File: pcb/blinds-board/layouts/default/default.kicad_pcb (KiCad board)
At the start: 6 copper layers, 38 x 81 mm, 87 parts

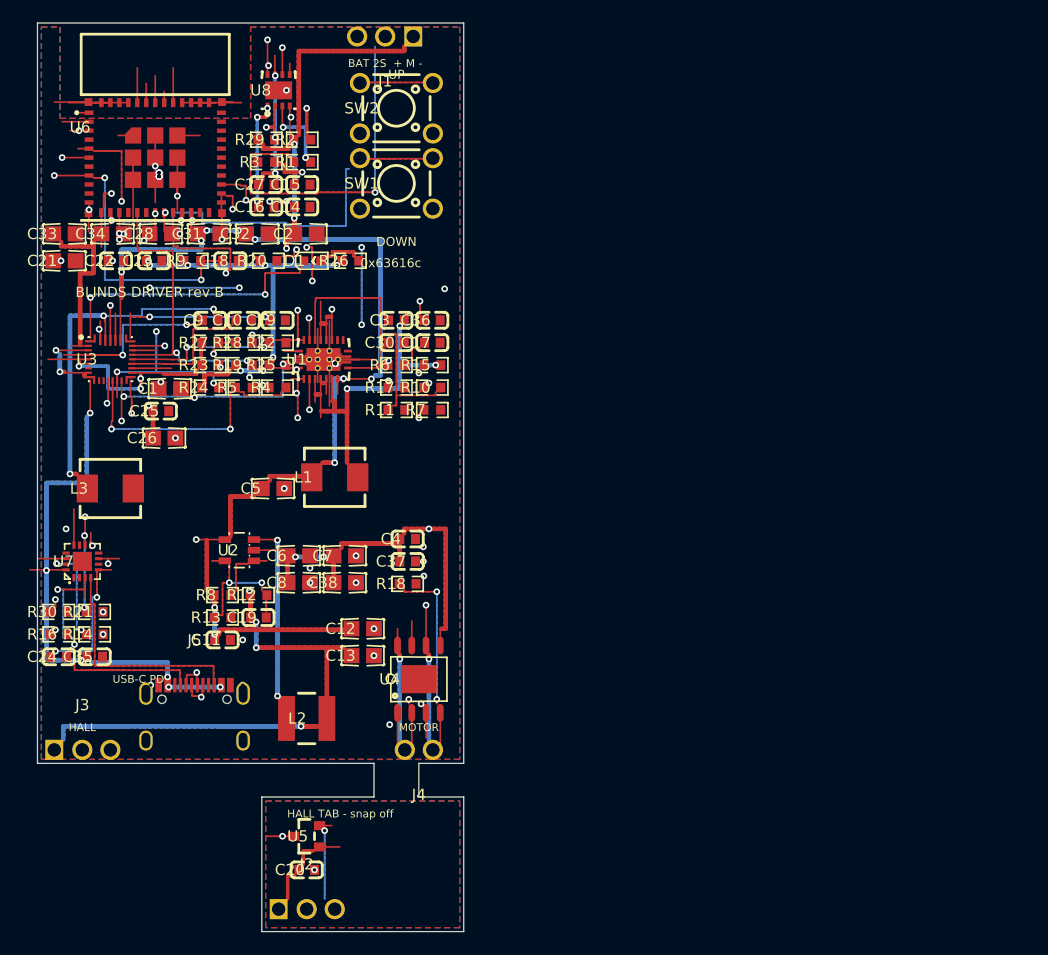
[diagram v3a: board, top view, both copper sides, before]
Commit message: feat(blinds-pcb): rev C — 88x32 flat board for the v2 center-drop unit
Board reshaped to lie flat on the enclosure floor: buttons + USB-C out
the front edge (unit x 38/49/60), hall tab moves below the board
(panel 88x47), 3x M3 mount holes + a B.Cu keep-out where the enclosure
pillar presses under the USB. Charger rotated 180 so its SW pins face
the inductor; flank passives mirrored to match; per-pad fanout
staggers re-derived (rev B's were orientation-specific). Netless pad
halos widened to via-hole clearance. Fully routed: 62 nets, ~10.2k
segments, 249 vias, zero unrouted.

KiCad DRC: 35 violations — SAME classes and slightly fewer than the
committed rev B board scores under today's harness (39), including the
identical 4 padstack_invalid on the BQ25798 corner pads and the
unconnected-pads artifact class. The DRC gate in build_outputs.sh
cannot currently pass on either rev; needs its own investigation
before gerbers.
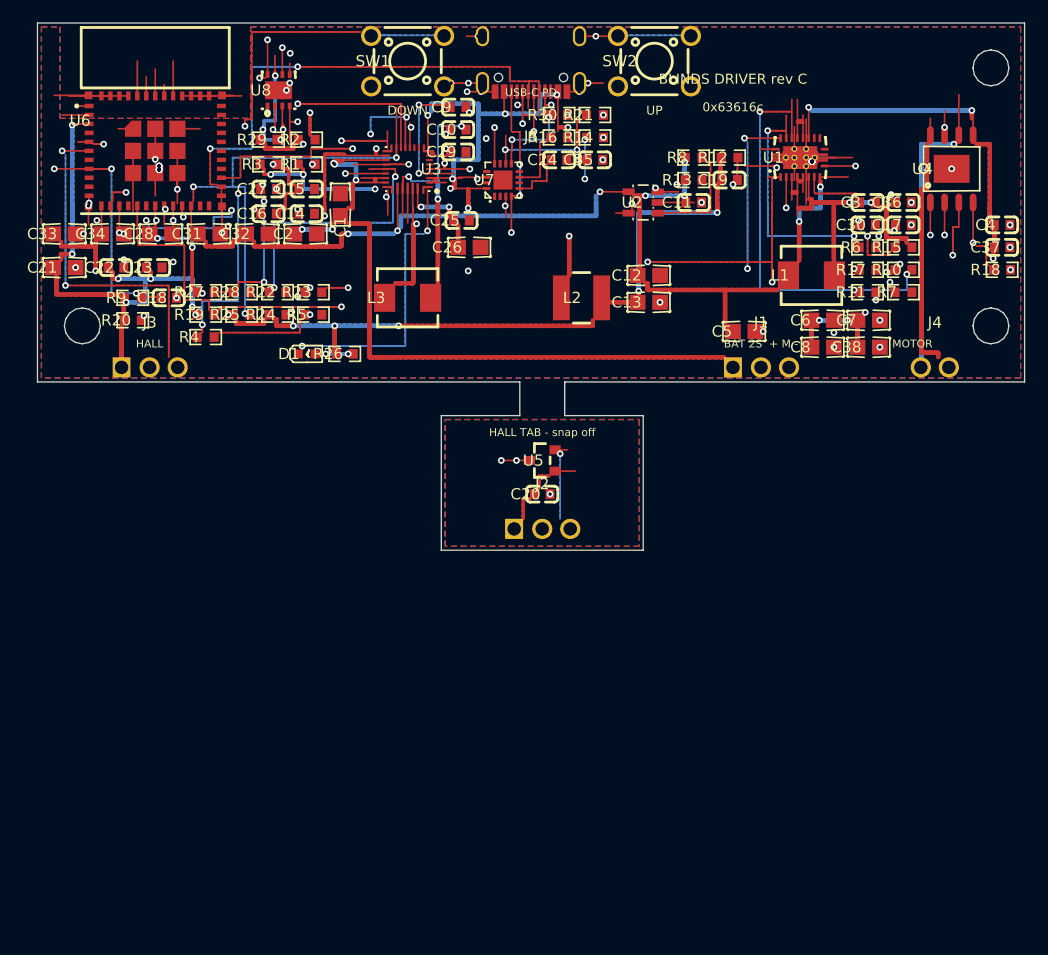
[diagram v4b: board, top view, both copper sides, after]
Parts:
- moved U4 65.8 mm to (81.5, 13.0)
- moved J5 65.2 mm to (44.0, 3.65), turned to 180 degrees
- moved C24 62.9 mm to (46.5, 12.2)
- moved C35 62.9 mm to (49.7, 12.2)
- moved R14 62.9 mm to (49.7, 10.2)
- moved R16 62.9 mm to (46.5, 10.2)
- moved R21 62.9 mm to (49.7, 8.20)
- moved R30 62.9 mm to (46.5, 8.20)
- moved C37 59.9 mm to (86.0, 20.0)
- moved C4 59.9 mm to (86.0, 18.0)
- moved R18 59.9 mm to (86.0, 22.0)
- moved C11 57.3 mm to (58.5, 16.0)
- moved C19 57.3 mm to (61.7, 14.0)
- moved R12 57.3 mm to (61.7, 12.0)
- moved R13 57.3 mm to (58.5, 14.0)
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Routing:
- net en_bst: track 43.6 -> 81.6 mm, vias 4 -> 5
- net usb_dp: track 77.2 -> 40.5 mm
- net batmid: track 31.6 -> 60.7 mm, vias 1 -> 3
- net hall_do: track 58.5 -> 29.7 mm, vias 1 -> 2
- net btn_up: track 44.9 -> 73.1 mm, vias 1 -> 4
- net VBUS: track 70.3 -> 93.9 mm, vias 9 -> 10
- net 2-2: track 2.40 -> 22.6 mm, vias 0 -> 3
- net usb_dn: track 64.4 -> 48.1 mm, vias 4 -> 2
- net chg_ce: track 22.4 -> 38.2 mm, vias 2 -> 3
- net chg_int: track 26.8 -> 42.0 mm
- net scl: track 28.3 -> 43.0 mm, vias 4 -> 3
- net ov_out: track 45.8 -> 31.4 mm, vias 3 -> 4
- net mot_a: track 11.2 -> 25.6 mm, vias 2 -> 1
- net 1-6: track 33.0 -> 47.0 mm, vias 4 -> 9
- net 1: track 58.8 -> 72.6 mm, vias 5 -> 6
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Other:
- board size 38 x 81 mm -> 88 x 47 mm
- board text added: "BLINDS DRIVER rev C"
- board text removed: "BLINDS DRIVER rev B"
